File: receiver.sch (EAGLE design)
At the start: 17 parts

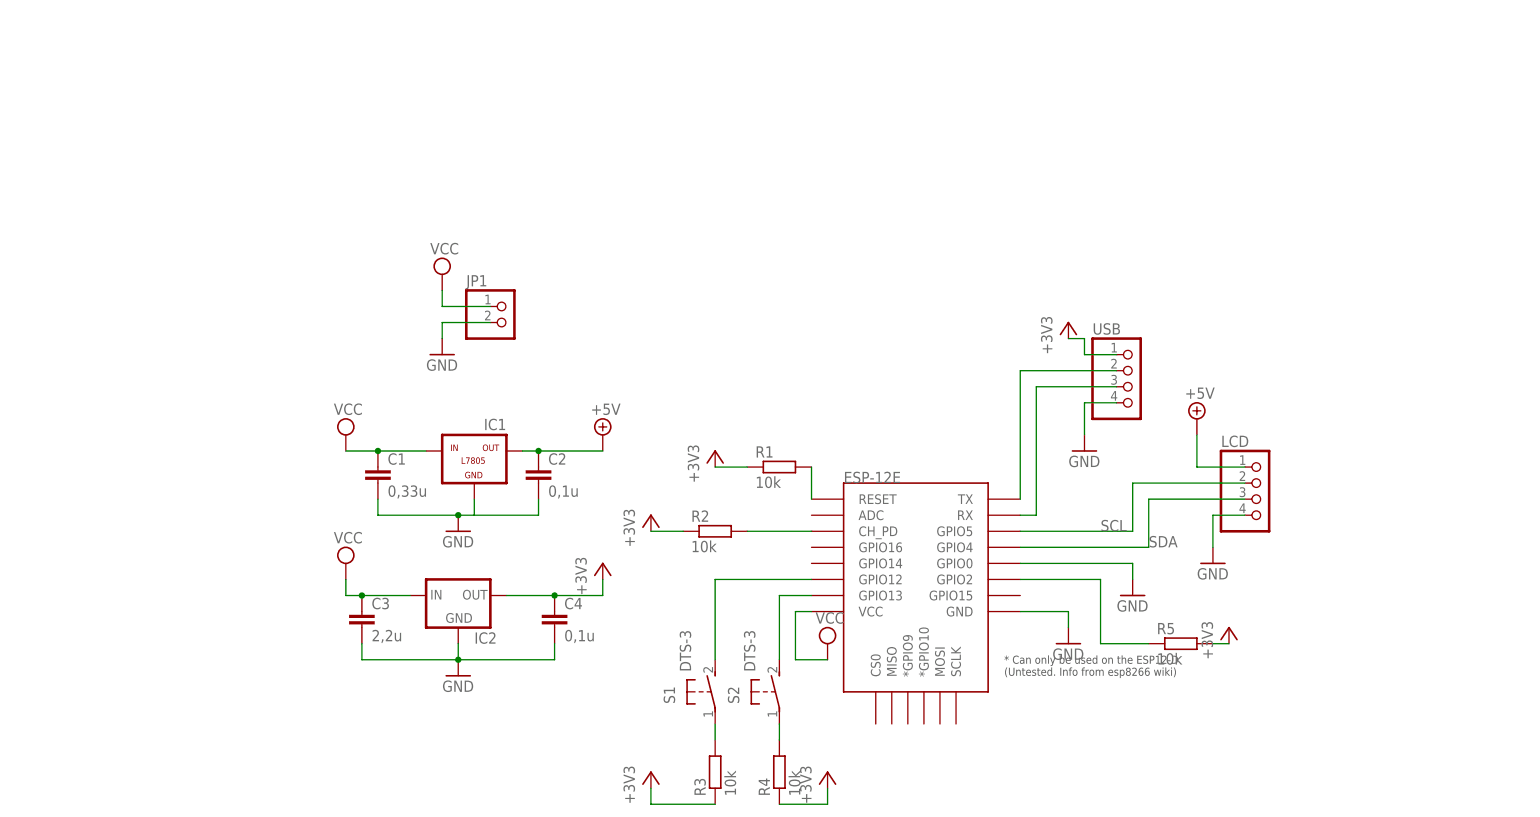
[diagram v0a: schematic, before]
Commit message: Improved some bugs in receiver's and survey's schematic.
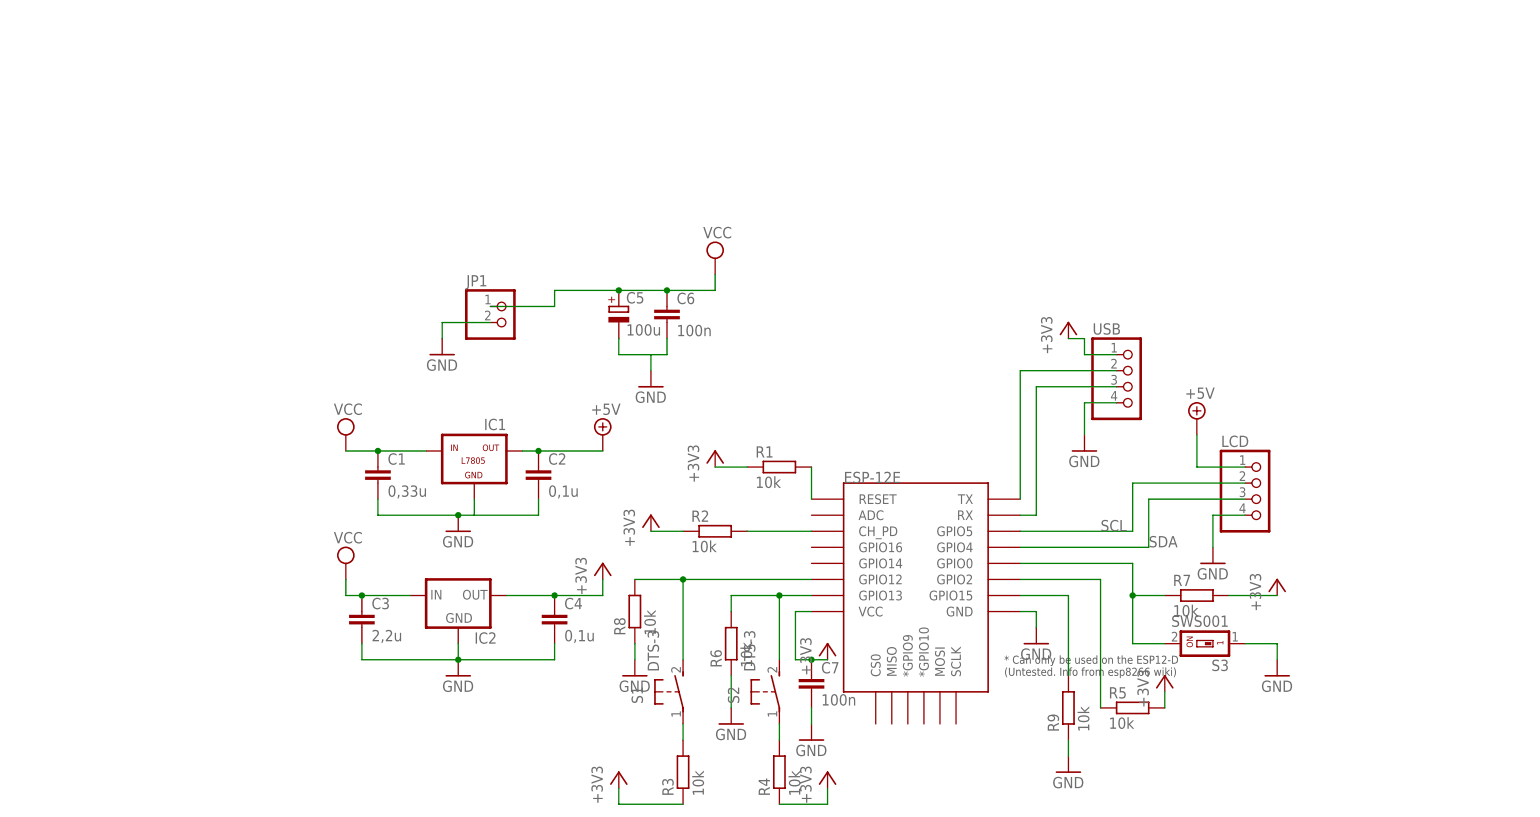
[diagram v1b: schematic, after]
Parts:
- added C5: 100u, rcl:CPOL-EUE2.5-6
- added C6, C7: 100n, rcl:C-EU025-025X050
- added R6, R7, R8, R9: 10k, rcl:R-EU_0204/5
- added S3: SWS001, smd-special:SWS001
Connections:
- new net N$11: ESP-12E.GPIO15, R9.2
- new net N$3: ESP-12E.GPIO0, R7.1, S3.2
- net +3V3: now also C7.1, ESP-12E.VCC, R7.2
- net GND: now also C5.-, C6.2, C7.2, R6.1, R8.1, R9.1, S3.1; no longer ESP-12E.GPIO0
- net N$10: now also R6.2
- net N$9: now also R8.2
- net VCC: now also C5.+, C6.1; no longer ESP-12E.VCC
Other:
- moved on the sheet: R3, R5, S1

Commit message: Corrected VCC pin connection, added level shifter to communicate micro controller with LCD, changed voltage supply marks, corrected connections of buttons to micro controller, added library with level shifter.
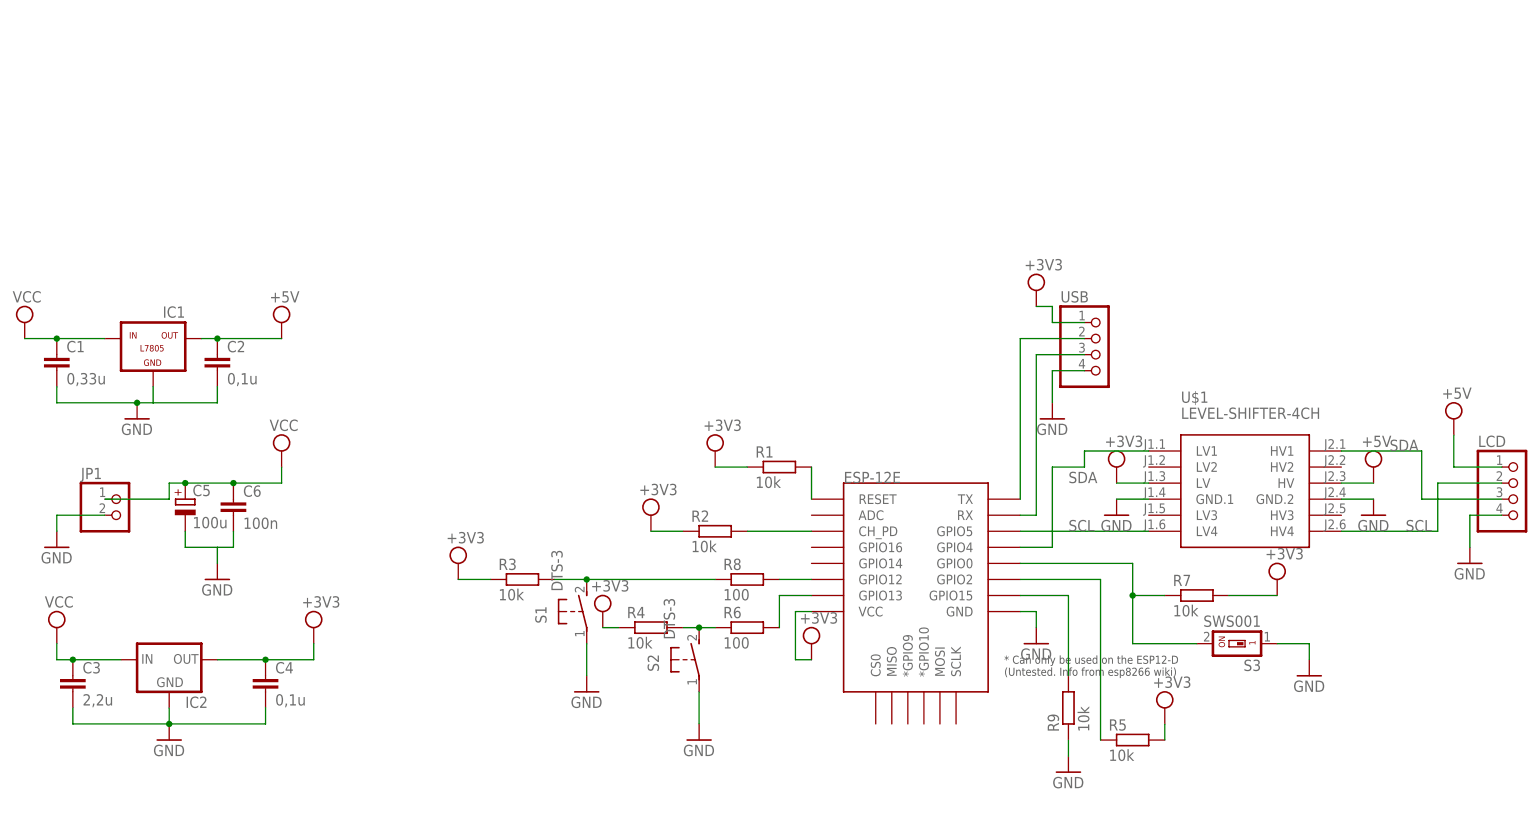
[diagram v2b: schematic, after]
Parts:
- removed C7: 100n, rcl:C-EU025-025X050
- added U$1: LEVEL-SHIFTER-4CH, diy-modules:LEVEL-SHIFTER-4CH
- R6, R8: value 10k -> 100
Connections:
- removed net +3V3: C4.1, C7.1, ESP-12E.VCC, IC2.OUT, R1.1, R2.1, R3.1, R4.1, R5.2, R7.2, USB.1
- removed net +5V: C2.1, IC1.OUT, LCD.1
- net GND: now also S1.1, S2.1, U$1.GND.1, U$1.GND.2; no longer C7.2, R6.1, R8.1
- net N$10: no longer S2.2
- net N$7: now also ESP-12E.GPIO12, R8.2; no longer R3.2, S1.1
- net N$8: now also R6.1, S2.2; no longer S2.1
- net N$9: now also R3.2, R8.1; no longer ESP-12E.GPIO12, R8.2
- net SCL: now also U$1.HV4, U$1.LV4
- net SDA: now also U$1.HV1, U$1.LV1
- net VCC: now also C2.1, C4.1, ESP-12E.VCC, IC1.OUT, IC2.OUT, LCD.1, R1.1, R2.1, R3.1, R4.1, R5.2, R7.2, U$1.HV, U$1.LV, USB.1
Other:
- moved on the sheet: C1, C2, C3, C4, C5, C6, IC1, IC2, JP1, LCD, R3, R4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

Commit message: Added to receiver pull-up resitors, added documentation of LCD, corrected reset pin connection.
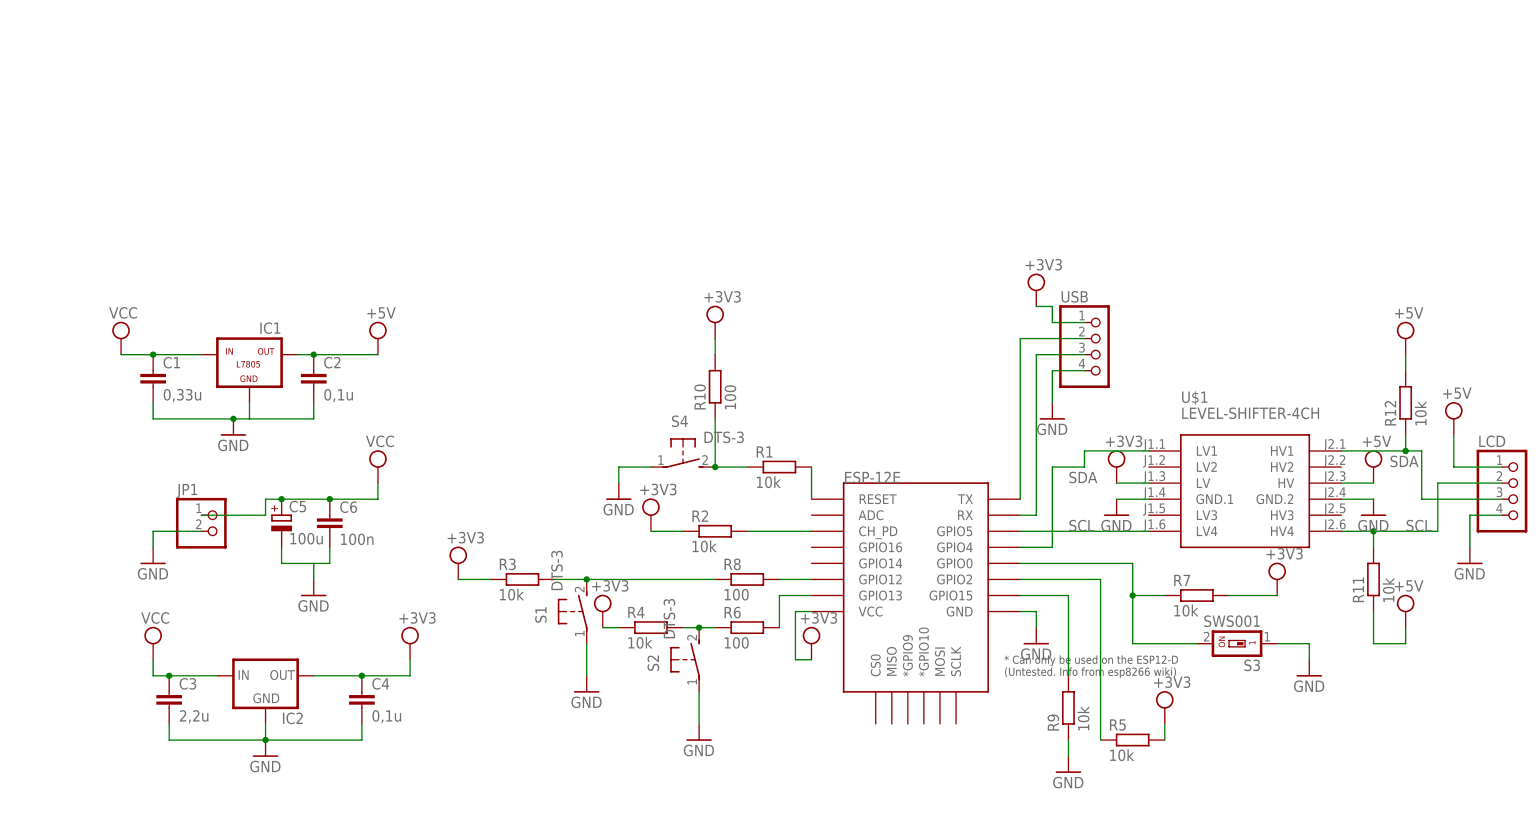
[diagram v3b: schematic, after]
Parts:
- added R10: 100, rcl:R-EU_0204/5
- added R11, R12: 10k, rcl:R-EU_0204/5
- added S4: DTS-3, switch-tact:DTS-3
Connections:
- new net N$12: R1.1, R10.1, S4.2
- net GND: now also S4.1
- net SCL: now also R11.2
- net SDA: now also R12.1
- net VCC: now also R10.2, R11.1, R12.2; no longer R1.1
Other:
- moved on the sheet: C1, C2, C3, C4, C5, C6, IC1, IC2, JP1

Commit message: Corrected Reset pin connection, changed stablizer on step yp/step down converter.
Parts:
- R11, R12: value 10k -> 4,7k
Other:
- moved on the sheet: C1, C2, C3, C4, C5, C6, IC1, IC2, JP1
